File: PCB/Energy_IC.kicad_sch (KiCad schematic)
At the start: 1 part, among them U2 ATM90E26-YU

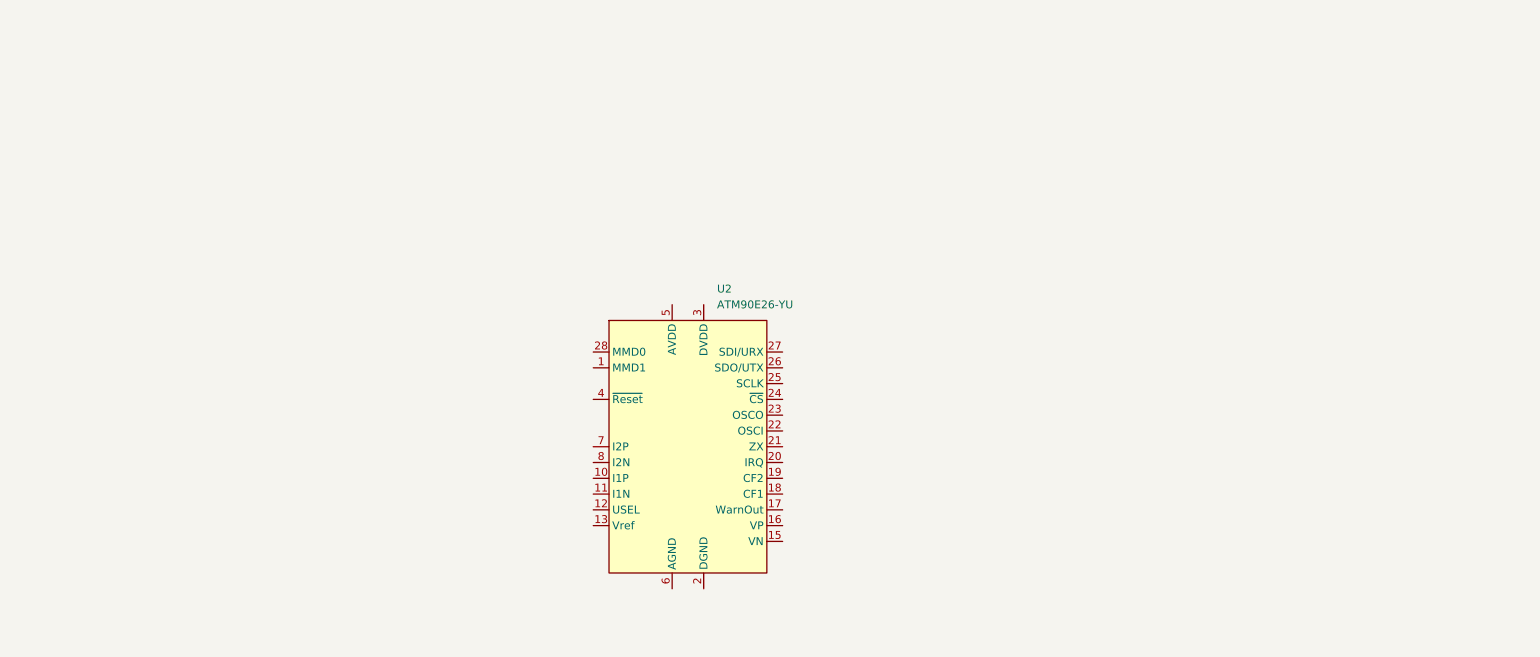
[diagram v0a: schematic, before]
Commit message: added firmware dir
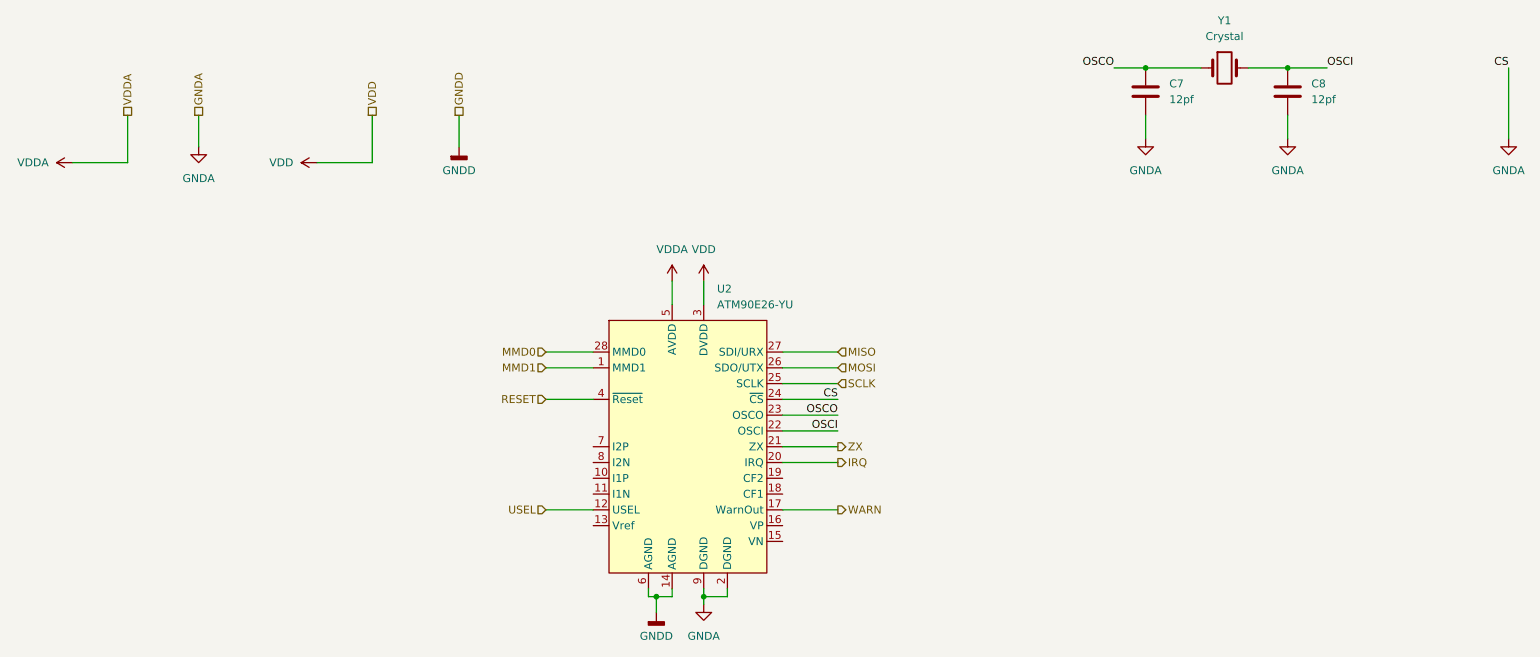
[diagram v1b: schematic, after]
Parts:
- added C7, C8: 12pf, symbol Device:C
- added Y1: Crystal, symbol Device:Crystal
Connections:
- net MMD1: now reaches U2.1 (MMD1)
- net USEL: now reaches U2.12 (USEL)
- net GNDD: now reaches U2.14 (AGND), U2.6 (AGND)
- net WARN: now reaches U2.17 (WarnOut)
- net GNDA: now reaches U2.2 (DGND), U2.9 (DGND)
- net GNDA: now also U2.24 (~{CS}), C7.2, C8.2
- net IRQ: now reaches U2.20 (IRQ)
- net ZX: now reaches U2.21 (ZX)
- net OSCI: now reaches U2.22 (OSCI)
- net OSCI: now also C8.1, Y1.2
- net OSCO: now reaches U2.23 (OSCO)
- net OSCO: now also C7.1, Y1.1
- net SCLK: now reaches U2.25 (SCLK)
- net MOSI: now reaches U2.26 (SDO/UTX)
- net MISO: now reaches U2.27 (SDI/URX)
- net MMD0: now reaches U2.28 (MMD0)
- net VDD: now reaches U2.3 (DVDD)
- net RESET: now reaches U2.4 (~{Reset})
- net VDDA: now reaches U2.5 (AVDD)
